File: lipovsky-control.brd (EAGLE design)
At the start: 56.2 x 21 mm, 12 parts, among them U1 ATTINYX4A8MU, U10 CCR20MA_45V, U7 LTV-816S

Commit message: .
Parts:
- moved D61 69.3 mm to (50.1, 26.8), turned to 90 degrees
- moved D51 64.5 mm to (46.7, 26.8), turned to 90 degrees
- moved D41 59.7 mm to (43.3, 26.8), turned to 90 degrees
- moved D31 54.9 mm to (39.9, 26.8), turned to 90 degrees
- moved D21 50.1 mm to (36.5, 26.8), turned to 90 degrees
- moved D11 45.3 mm to (33.1, 26.8), turned to 90 degrees
- moved U10 40.1 mm to (29.4, 27.6), turned to 90 degrees
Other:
- board size 56.2 x 21 mm -> 57 x 32 mm

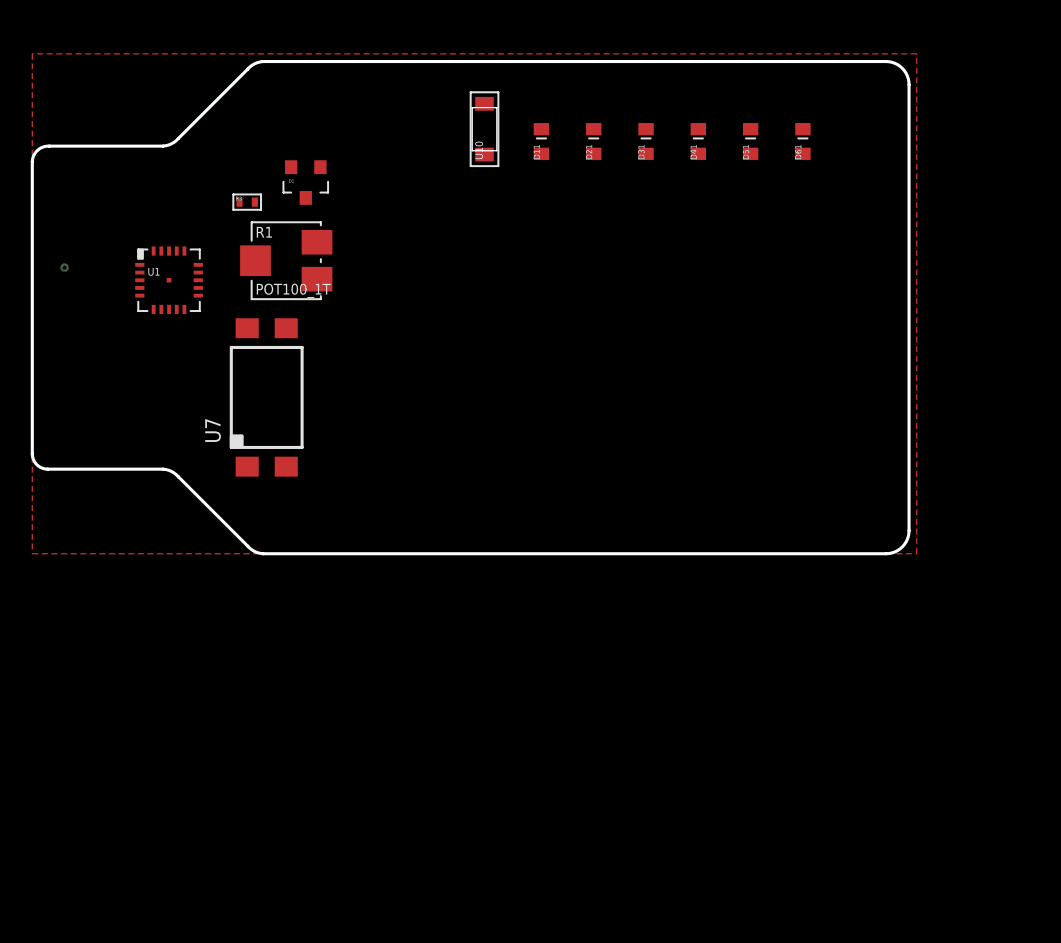
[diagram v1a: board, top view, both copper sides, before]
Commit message: moving boosters
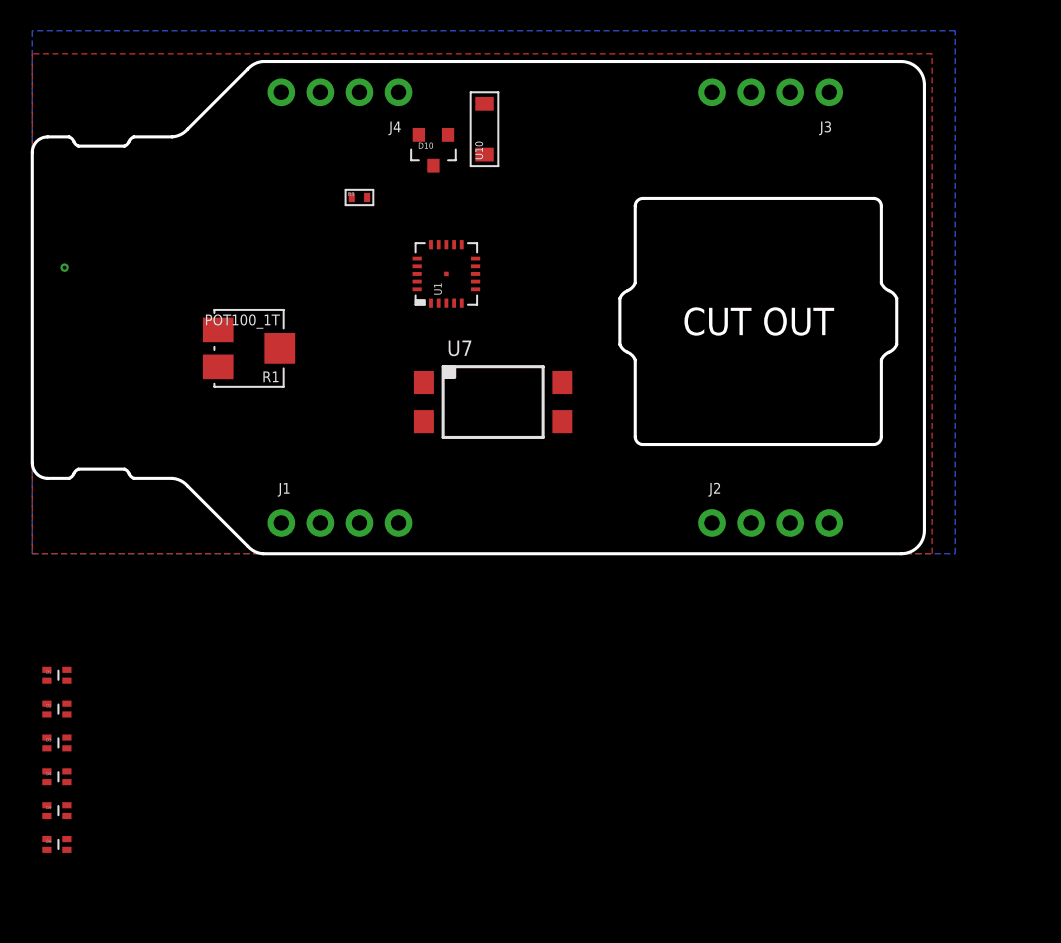
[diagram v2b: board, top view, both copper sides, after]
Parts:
- removed D11, D21, D31, D41, D51, D61: LEDGREEN_2V_30MA, dubec:0603+
- added D10: D_ZENER3V, dubec:SOT23-3
- added D2, D3, D4, D5, D6: LED_DUALGO, dubec:0603+DUAL
- added J1, J2, J3, J4: M04-929P, dubec:1X04_929P
- D1: value D_ZENER3V -> LED_DUALGO; device dubec:SOT23-3 -> dubec:0603+DUAL
- moved D1 35.9 mm to (1.60, -7.90)
- moved U1 18.0 mm to (26.9, 18.2), turned to 90 degrees
- moved U7 14.7 mm to (30.0, 9.86), turned to 270 degrees
- moved R3 7.31 mm to (21.3, 23.2)
- moved R1 6.19 mm to (14.1, 13.3), turned to 180 degrees
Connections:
- removed net N$11: U1.14
- removed net N$17: D11.C
- removed net N$18: D41.C
- removed net N$4: U1.4
- removed net N$9: D31.C
- new net !OE: J3.2, U1.11
- new net BATT-: J1.2
- new net CP: J3.3, U1.12
- new net D1: D1.A2, D1.C1, D2.A2, D2.C1, D3.A2, D3.C1
- new net DS: J3.4, U1.14
- new net Q7S: J1.4
- new net S+: J4.2
- new net SFB: J1.3, U1.4
- new net VCC_REG: J4.4
- net FB: now also J2.4
- net N$1: now also D10.3; no longer D1.3
- net N$12: now also D6.C1; no longer U1.12
- net N$13: now also D5.C1; no longer U1.11
- net N$16: now also D4.C1; no longer D21.C
- net N$2: no longer D11.A, D21.A, D31.A, D41.A, D51.A, D61.A
- net OPTO_A: now also J2.2
- net OPTO_C: now also J2.3
- net S-: now also D10.1, J1.1, J2.1, J3.1, J4.1; no longer D1.1
- net VCC: now also J4.3
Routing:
- added copper zone on layer 16, net BATT-
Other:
- board size 57 x 32 mm -> 58 x 32 mm
- board text added: "CUT OUT"

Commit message: .
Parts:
- removed D1, D4, D5, D6: LED_DUALGO, dubec:0603+DUAL
- added C1, C21, C31: CAP4.7U_6.3V, dubec:0603
- added C22, C32: CAP22U_10V, dubec:0603
- added D13, D14, D15, D16, D17, D18: LED_DUALGO, dubec:0603+DUAL
- added I2, I3: (no value), dubec:0603
- added R2: RES15.4K_16, dubec:0402
- added R4, R5: RES5.1K_16, dubec:0402
- added R6: RES27.4K_16, dubec:0402
- added U2, U3: MIC2288YD5, dubec:SOT-23-5
- D2, D3: value LED_DUALGO -> D_SCH20V_0.5A; device dubec:0603+DUAL -> dubec:SOD523+
- moved D2 35.8 mm to (17.9, 21.8), turned to 270 degrees
- moved D3 35.4 mm to (10.9, 21.8), turned to 270 degrees
- moved D10 12.7 mm to (26.6, 13.5), turned to 90 degrees
- moved R3 12.0 mm to (30.7, 15.8), turned to 90 degrees
- moved R1 11.7 mm to (25.0, 9.00)
- moved U10 4.26 mm to (32.1, 24.3)
- moved U7 2.21 mm to (32.0, 9.00), turned to 0 degrees
- moved U1 1.68 mm to (27.4, 19.8)
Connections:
- new net N$11: R5.2, R6.1, U3.3
- new net N$17: R2.1, R4.2, U2.3
- new net N$4: D2.A, I2.2
- new net N$9: D3.A, I3.2
- net D1: now also D13.A2, D13.C1, D14.A2, D14.C1, D15.A2, D15.C1; no longer D1.A2, D1.C1, D2.A2, D2.C1, D3.A2, D3.C1
- net N$12: now also D16.C1; no longer D6.C1
- net N$13: now also D17.C1; no longer D5.C1
- net N$16: now also D18.C1; no longer D4.C1
- net S+: now also C21.2, C31.2, I2.1, I3.1, U2.4, U2.5, U3.4, U3.5
- net S-: now also C21.1, C22.1, C31.1, C32.1, R4.1, R5.1, U2.2, U3.2
- net VCC: now also C22.2, D2.C, R2.2, U2.1
- net VCC_REG: now also C32.2, D3.C, R6.2, U3.1
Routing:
- net VCC: track 0.00 -> 5.83 mm
- net S-: track 0.00 -> 5.82 mm
- net S+: track 0.00 -> 5.53 mm
- net N$17: track 0.00 -> 3.06 mm
- net N$4: track 0.00 -> 1.13 mm
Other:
- board size 58 x 32 mm -> 59 x 32 mm

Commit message: .
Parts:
- R2: value RES15.4K_16 -> RES14.3K_16
- R4, R5: value RES5.1K_16 -> RES4.7K_16
- R6: value RES27.4K_16 -> RES25.5K_16
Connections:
- net N$4: now also U2.1
- net N$9: now also U3.1
- net VCC: no longer U2.1
- net VCC_REG: no longer U3.1
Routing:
- net N$4: track 1.13 -> 2.79 mm
- net VCC: track 5.83 -> 4.18 mm
- net S-: track 5.82 -> 5.96 mm, vias 0 -> 2
- net S+: vias 0 -> 2

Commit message: LED matrix
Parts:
- removed D13, D14, D15, D16, D17, D18: LED_DUALGO, dubec:0603+DUAL
- removed U10: CCR20MA_45V, dubec:SOD-123
- added D101, D102, D103, D104, D105, D106, D4, D5, D6: LED_DUALRG-2, dubec:1206+DUAL
- added U$1, U$2: CCR10MA, dubec:SOD-123
- moved C21 1.87 mm to (23.9, 24.8)
- moved C22 1.87 mm to (20.5, 20.4)
- moved C32 1.87 mm to (13.5, 20.4)
- moved D2 1.87 mm to (19.8, 22.3)
- moved D3 1.87 mm to (12.8, 22.3)
- moved I3 1.87 mm to (12.7, 24.8)
- moved R2 1.87 mm to (22.3, 20.2)
- moved R4 1.87 mm to (23.8, 22.6)
- moved R5 1.87 mm to (16.8, 22.6)
- moved R6 1.87 mm to (15.3, 20.2)
- moved U2 1.87 mm to (21.8, 23.5)
- moved U3 1.87 mm to (14.8, 23.5)
- moved C31 1.87 mm to (16.9, 24.8)
- moved I2 1.87 mm to (19.6, 24.8)
- renumbered D10 to D1
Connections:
- removed net C1: U10.A
- removed net N$12: D16.C1
- removed net N$13: D17.C1
- removed net N$16: D18.C1
- removed net N$2: U10.C
- new net D2: D104.A2, D104.C1, D105.A2, D105.C1, D106.A2, D106.C1
- new net D3: D4.A2, D4.C1, D5.A2, D5.C1, D6.A2, D6.C1
- new net D4: D101.A1, D101.C2, D104.A1, D104.C2, D4.A1, D4.C2
- new net D5: D102.A1, D102.C2, D105.A1, D105.C2, D5.A1, D5.C2
- new net D6: D103.A1, D103.C2, D106.A1, D106.C2, D6.A1, D6.C2
- net D1: now also D101.A2, D101.C1, D102.A2, D102.C1, D103.A2, D103.C1; no longer D13.A2, D13.C1, D14.A2, D14.C1, D15.A2, D15.C1

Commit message: .
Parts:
- removed D1: D_ZENER3V, dubec:SOT23-3
- removed D6: LED_DUALRG-2, dubec:1206+DUAL
- removed U$1, U$2: CCR10MA, dubec:SOD-123
- added C2: CAP470N_10V, dubec:0402
- added C3: CAP47N_50V, dubec:0402
- added R10, R11, R12, R7, R8, R9: RES150_10, dubec:0603
- added R13, R14: RES330_16, dubec:0402
- R1: value POT100_1T -> POT5K; device dubec:ST-4EA -> dubec:3296W
- R3: value RES590_16 -> RES330_16
- moved C1 15.8 mm to (21.4, 15.6)
- moved I3 14.9 mm to (26.9, 29.3)
- moved C31 14.9 mm to (31.1, 29.3)
- moved C32 14.9 mm to (27.7, 24.9)
- moved D3 14.9 mm to (26.9, 26.8)
- moved R5 14.9 mm to (31.0, 27.1)
- moved R6 14.9 mm to (29.5, 24.7)
- moved U3 14.9 mm to (29.0, 28.0)
- moved C22 13.9 mm to (33.7, 24.9)
- moved D2 13.9 mm to (33.0, 26.8)
- moved I2 13.9 mm to (32.9, 29.3)
- moved C21 13.9 mm to (37.1, 29.3)
- moved R2 13.9 mm to (35.5, 24.7)
- moved R4 13.9 mm to (37.0, 27.1)
- moved U2 13.9 mm to (35.0, 28.0)
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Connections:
- net N$10 renamed !RESET
- net VCC_REG renamed +8V
- removed net D5: D102.A1, D102.C2, D105.A1, D105.C2, D5.A1, D5.C2
- removed net D6: D103.A1, D103.C2, D106.A1, D106.C2, D6.A1, D6.C2
- removed net N$14: U1.15
- removed net N$15: U1.16
- removed net N$3: U1.5
- removed net SFB: J1.3, U1.4
- removed net VCC: C22.2, D2.C, J4.3, R2.2, R3.2, U1.9
- new net +5V: C1.2, C22.2, D2.C, J4.3, R12.1, R2.2, U1.9, U7.4
- new net D_OVERTEMP: D5.A1, D5.C2, U1.15
- new net D_STATUS: D4.A1, D4.C2, U1.16
- new net FB_ADC: C3.2, R14.1, U1.4
- new net N$2: D4.A2, D4.C1, D5.A2, D5.C1, R11.2, R12.2
- new net S_ADC: C2.1, R13.2, U1.5
- net D1: now also D101.A1, D101.C2, D102.A1, D102.C2, D103.A1, D103.C2, R7.1; no longer D101.A2, D101.C1, D102.A2, D102.C1, D103.A2, D103.C1
- net D2: now also D101.A2, D101.C1, D104.A1, D104.C2, D105.A1, D105.C2, R8.1; no longer D104.A2, D104.C1, D105.A2, D105.C1, D106.A2, D106.C1
- net D3: now also D102.A2, D102.C1, D104.A2, D104.C1, D105.A2, D105.C1, D106.A1, D106.C2, R9.1; no longer D4.A2, D4.C1, D5.A2, D5.C1, D6.A2, D6.C1
- net D4: now also D103.A2, D103.C1, D106.A2, D106.C1, R10.1; no longer D101.A1, D101.C2, D104.A1, D104.C2, D4.A1, D4.C2
- net FB: now also R14.2, R3.2; no longer R1.2
- net N$1: now also R1.WIPER; no longer D1.3, U7.4
- net N$5: now also R7.2
- net N$6: now also R8.2
- net N$7: now also R9.2
- net N$8: now also R10.2
- net S+: now also R13.1
- net S-: now also C1.1, C2.2, C3.1, R1.CW, R11.1; no longer D1.1, R1.3
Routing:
- net VCC: track 4.18 -> 0.00 mm
- net +5V: track 0.00 -> 4.18 mm

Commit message: .
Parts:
- added J5: AVRISPWR, dubec:WR-BHD-3X2
- added R15: RES10K_16, dubec:0402
- moved D5 13.8 mm to (13.5, 21.0)
- moved R10 10.8 mm to (13.5, 10.2), turned to 180 degrees
- moved R9 9.65 mm to (13.5, 8.90), turned to 180 degrees
- moved D4 9.09 mm to (13.5, 18.5)
- moved R3 8.72 mm to (29.8, 22.3), turned to 90 degrees
- moved R8 8.46 mm to (13.5, 7.60), turned to 180 degrees
- moved U1 7.40 mm to (18.0, 7.90), turned to 180 degrees
- moved R7 7.27 mm to (13.5, 6.30), turned to 180 degrees
- moved R14 6.54 mm to (28.8, 22.3), turned to 270 degrees
- moved R11 6.36 mm to (24.7, 11.2)
- moved R12 6.15 mm to (24.7, 9.90)
- moved C1 5.64 mm to (18.0, 11.1), turned to 180 degrees
- moved C3 5.13 mm to (27.8, 22.3), turned to 90 degrees
- moved R13 4.15 mm to (36.4, 21.6), turned to 270 degrees
- moved C2 3.34 mm to (35.4, 21.6), turned to 270 degrees
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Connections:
- removed net N$8: R10.2, U1.20
- new net N$3: R10.1, U1.11
- net !OE: now also J5.3, U1.1; no longer U1.11
- net !RESET: now also J5.5, R15.2
- net +5V: now also J5.2, R15.1
- net CP: now also J5.1, U1.20; no longer U1.12
- net D1: now also R7.2; no longer R7.1
- net D2: now also R8.2; no longer R8.1
- net D3: now also R9.2; no longer R9.1
- net D4: now also R10.2; no longer R10.1
- net DS: now also J5.4, U1.16; no longer U1.14
- net D_OVERTEMP: now also U1.2; no longer U1.15
- net D_STATUS: now also U1.3; no longer U1.16
- net N$5: now also R8.1, U1.14; no longer R7.2, U1.3
- net N$6: now also R7.1, U1.15; no longer R8.2, U1.2
- net N$7: now also R9.1, U1.12; no longer R9.2, U1.1
- net S-: now also J5.6
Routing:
- net D3: track 0.00 -> 30.4 mm, vias 0 -> 2
- net D2: track 0.00 -> 24.9 mm, vias 0 -> 2
- net D1: track 0.00 -> 24.0 mm
- net D4: track 0.00 -> 20.9 mm, vias 0 -> 2
- net S-: track 5.96 -> 18.0 mm
- net S+: track 5.53 -> 17.1 mm
- net +8V: track 0.00 -> 4.83 mm, vias 0 -> 1
- net N$11: track 0.00 -> 2.92 mm
- net N$9: track 0.00 -> 2.83 mm
- net N$7: track 0.00 -> 2.06 mm
- net N$5: track 0.00 -> 2.04 mm
- net !RESET: track 0.00 -> 0.90 mm, vias 0 -> 1
- net +5V: track 4.18 -> 4.83 mm, vias 0 -> 1
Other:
- board text added: "C1"
- board text added: "C2"
- board text added: "C3"
- board text added: "C4"
- board text added: "C5"
- board text added: "C6"
- board text added: "OK/ ERR"
- board text added: "OVER TEMP"

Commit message: redo
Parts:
- J5: value AVRISPWR -> AVRISP0.1"; device dubec:WR-BHD-3X2 -> dubec:2X03
- moved C2 18.5 mm to (23.8, 7.20)
- moved R13 18.5 mm to (24.8, 7.20), turned to 90 degrees
- moved C3 17.4 mm to (23.8, 5.40)
- moved R14 17.4 mm to (24.8, 5.40)
- moved R15 10.1 mm to (13.9, 5.15)
- moved D5 7.91 mm to (18.0, 14.5), turned to 90 degrees
- moved J5 5.22 mm to (20.0, 25.0)
- moved D4 4.03 mm to (14.0, 14.5), turned to 90 degrees
- moved R3 2.50 mm to (29.6, 19.8), turned to 180 degrees
- moved R11 2.14 mm to (23.0, 9.90), turned to 90 degrees
- moved U1 1.35 mm to (19.0, 7.00)
- moved C21 1.00 mm to (38.1, 29.3)
- moved C22 1.00 mm to (34.7, 24.9)
- moved C31 1.00 mm to (32.1, 29.3)
- moved C32 1.00 mm to (28.7, 24.9)
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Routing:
- net S-: track 18.0 -> 116.8 mm, vias 2 -> 6
- net +5V: track 4.83 -> 66.3 mm, vias 1 -> 2
- net DS: track 0.00 -> 57.6 mm, vias 0 -> 1
- net !OE: track 0.00 -> 55.3 mm, vias 0 -> 1
- net CP: track 0.00 -> 55.3 mm, vias 0 -> 1
- net FB: track 0.00 -> 45.1 mm, vias 0 -> 2
- net !RESET: track 0.90 -> 31.6 mm, vias 1 -> 3
- net S+: track 17.1 -> 44.8 mm
- net OPTO_C: track 0.00 -> 26.5 mm, vias 0 -> 1
- net OPTO_A: track 0.00 -> 21.4 mm
- net N$2: track 0.00 -> 19.4 mm
- net D_STATUS: track 0.00 -> 16.2 mm, vias 0 -> 2
- net D_OVERTEMP: track 0.00 -> 13.5 mm, vias 0 -> 3
- net +8V: track 4.83 -> 18.0 mm
- net N$1: track 0.00 -> 7.57 mm
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- added copper zone on layer 1, net S-
